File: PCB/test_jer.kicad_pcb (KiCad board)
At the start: 2 copper layers, 63.8 x 88 mm, 46 parts, among them J1 AudioJack2, J2 AudioJack2, Q1 BSS138, Q10 BSS84, Q11 BSS138, Q12 BSS84, Q13 BSS138, Q2 BSS84, Q3 BSS138, Q4 BSS84, Q5 BSS138, Q6 BSS84, Q7 BSS138, Q8 BSS84, Q9 BSS138, U1 Pico, U2 MAX481E

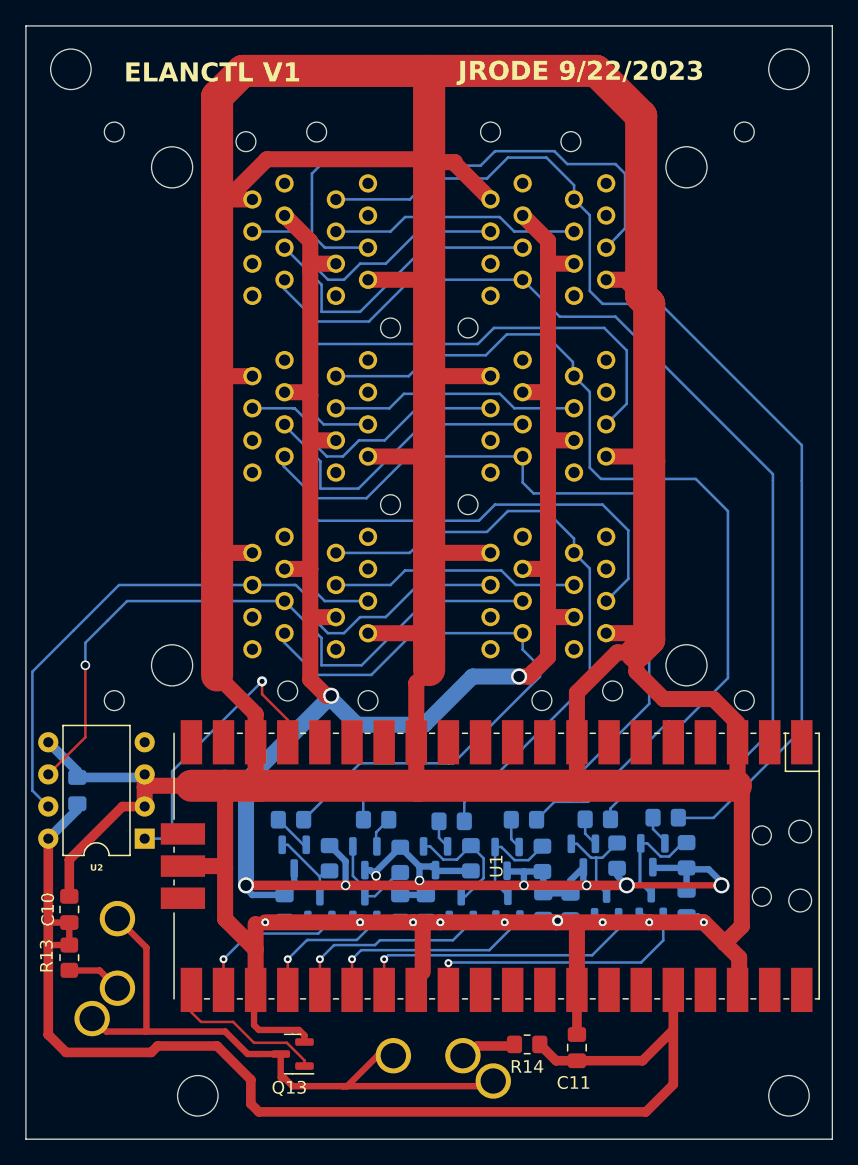
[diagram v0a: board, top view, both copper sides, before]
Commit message: Fixed switched source and drain on PMOS
On 12V common source amp for level shifter in subcircuit
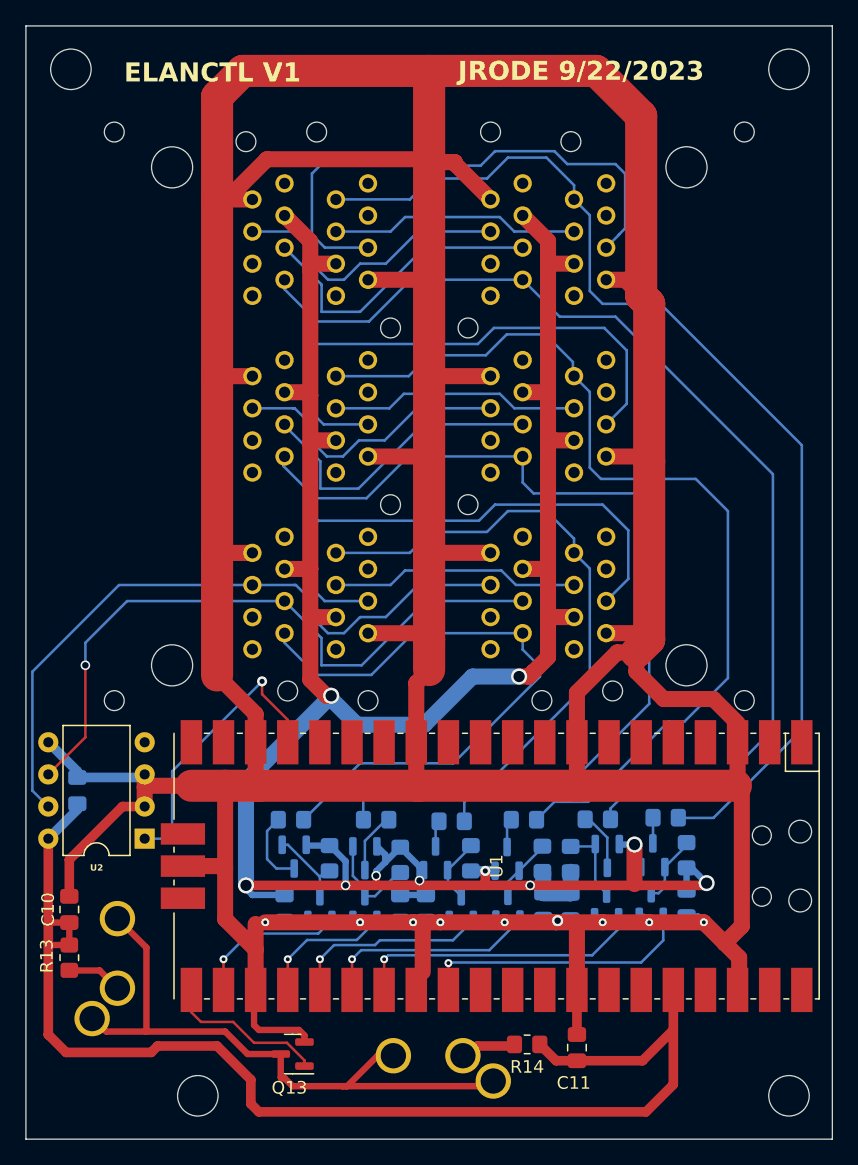
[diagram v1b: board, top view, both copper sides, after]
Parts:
- moved R3 3.68 mm to (83.5, 131.4)
- moved Q4 1.90 mm to (86.3, 131.2)
- turned Q2 to 90 degrees
- turned Q6 to 90 degrees
- turned Q8 to 90 degrees
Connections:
- Q10 pad 2: Net-(Q10-S) -> +12V
- Q10 pad 3: +12V -> Net-(Q10-D)
- Q12 pad 2: Net-(Q12-S) -> +12V
- Q12 pad 3: +12V -> Net-(Q12-D)
- Q2 pad 2: Net-(Q2-S) -> +12V
- Q2 pad 3: +12V -> Net-(Q2-D)
- Q4 pad 2: Net-(Q4-S) -> +12V
- Q4 pad 3: +12V -> Net-(Q4-D)
- Q6 pad 2: Net-(Q6-S) -> +12V
- Q6 pad 3: +12V -> Net-(Q6-D)
- Q8 pad 2: Net-(Q8-S) -> +12V
- Q8 pad 3: +12V -> Net-(Q8-D)
- R10 pad 1: Net-(Q10-S) -> Net-(Q10-D)
- R12 pad 1: Net-(Q12-S) -> Net-(Q12-D)
- R2 pad 1: Net-(Q2-S) -> Net-(Q2-D)
- R4 pad 1: Net-(Q4-S) -> Net-(Q4-D)
- R6 pad 1: Net-(Q6-S) -> Net-(Q6-D)
- R8 pad 1: Net-(Q8-S) -> Net-(Q8-D)
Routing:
- net +12V: track 220.5 -> 212.8 mm
- net Net-(Q12-D): track 0.00 -> 5.94 mm
- net Net-(Q10-D): track 0.00 -> 4.89 mm
- net Net-(Q7-D): track 9.98 -> 5.21 mm
- net Net-(Q4-D): track 0.00 -> 4.74 mm
- net Net-(Q5-D): track 8.91 -> 5.05 mm
- net Net-(Q12-S): track 3.03 -> 0.00 mm
- net Net-(Q1-D): track 8.44 -> 5.50 mm
- net Net-(Q10-S): track 2.46 -> 0.00 mm
- net Net-(Q6-S): track 2.42 -> 0.00 mm
- net Net-(Q6-D): track 0.00 -> 2.30 mm
- net Net-(Q4-S): track 2.27 -> 0.00 mm
- net Net-(Q8-S): track 2.27 -> 0.00 mm
- net Net-(Q2-S): track 2.23 -> 0.00 mm
- net Net-(Q8-D): track 0.00 -> 2.10 mm
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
